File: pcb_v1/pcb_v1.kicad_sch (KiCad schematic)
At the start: 18 parts, among them SW2 SW_Push, U2 SRV05-4, U3 IQS624-3200-DNR

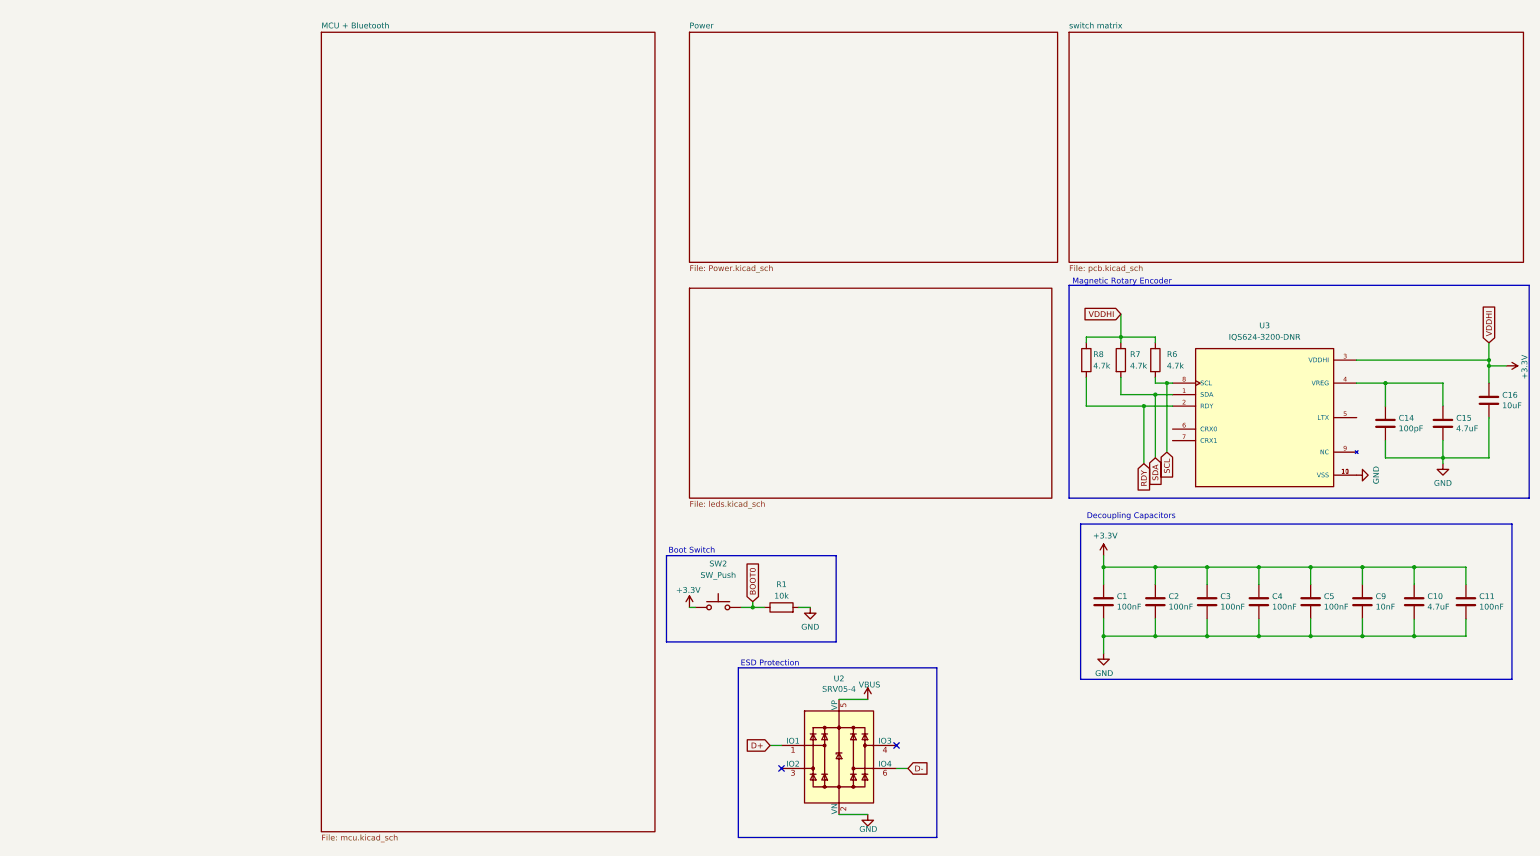
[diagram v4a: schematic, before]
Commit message: Connected OLED pin connector
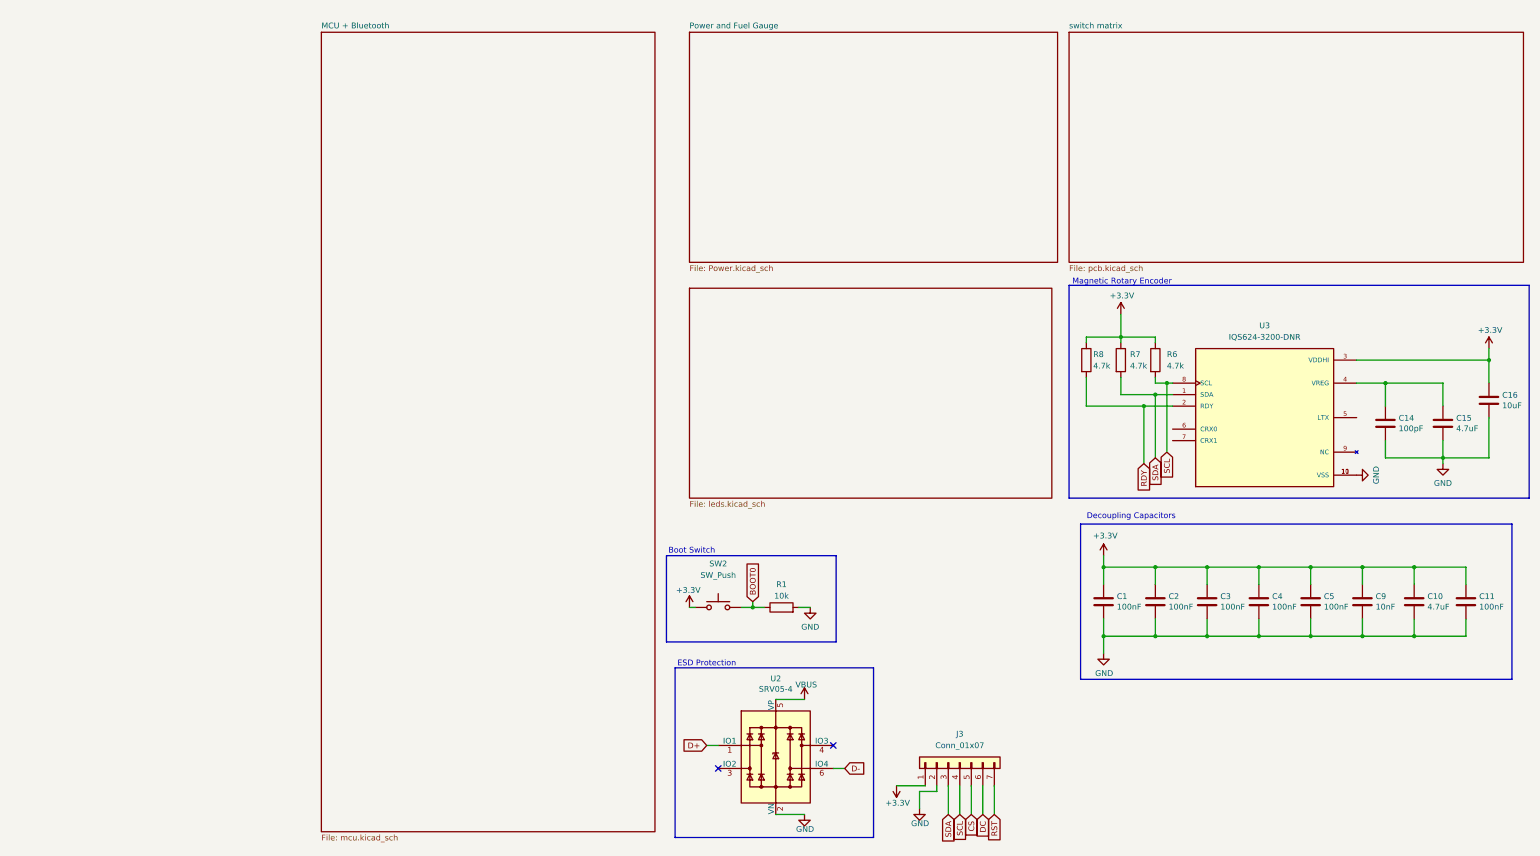
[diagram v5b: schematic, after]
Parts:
- added J3: Conn_01x07, Connector_JST:JST_SH_SM07B-SRSS-TB_1x07-1MP_P1.00mm_Horizontal, symbol Connector_Generic:Conn_01x07
- C1, C10, C11, C14, C15, C16, C2, C3, C4, C5, C9: footprint Murata Capacitor:CAPC1608X90N -> GRM1555C2A101GA01D:CAPC1005X55N
- R1, R6, R7, R8: footprint Yageo Resistor:RESC1607X60N -> RC0402FR-7D4K7L:RESC1005X40N
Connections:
- net +3.3V: now also J3.1 (Pin_1)
- net GND: now also J3.2 (Pin_2)
- net SCL: now also J3.4 (Pin_4)
- net SDA: now also J3.3 (Pin_3)
- new net CS: J3.5 (Pin_5)
- new net DC: J3.6 (Pin_6)
- new net RST: J3.7 (Pin_7)
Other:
- sheet Power renamed Power and Fuel Gauge
- moved on the sheet: U2

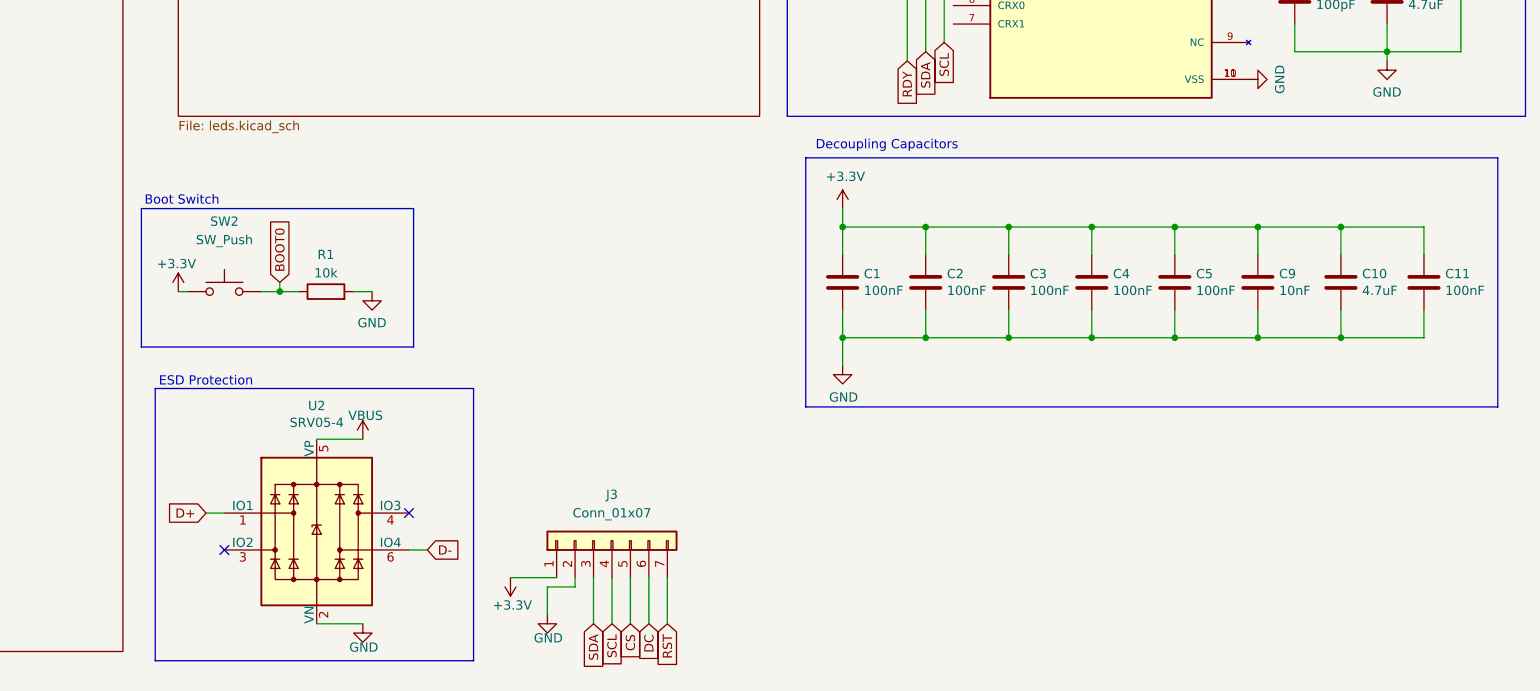
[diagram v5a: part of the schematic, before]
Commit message: Changed Layout of Keyboard
Row 1, Column 14 Removed due to OLED Screen taking up 2x2 u space
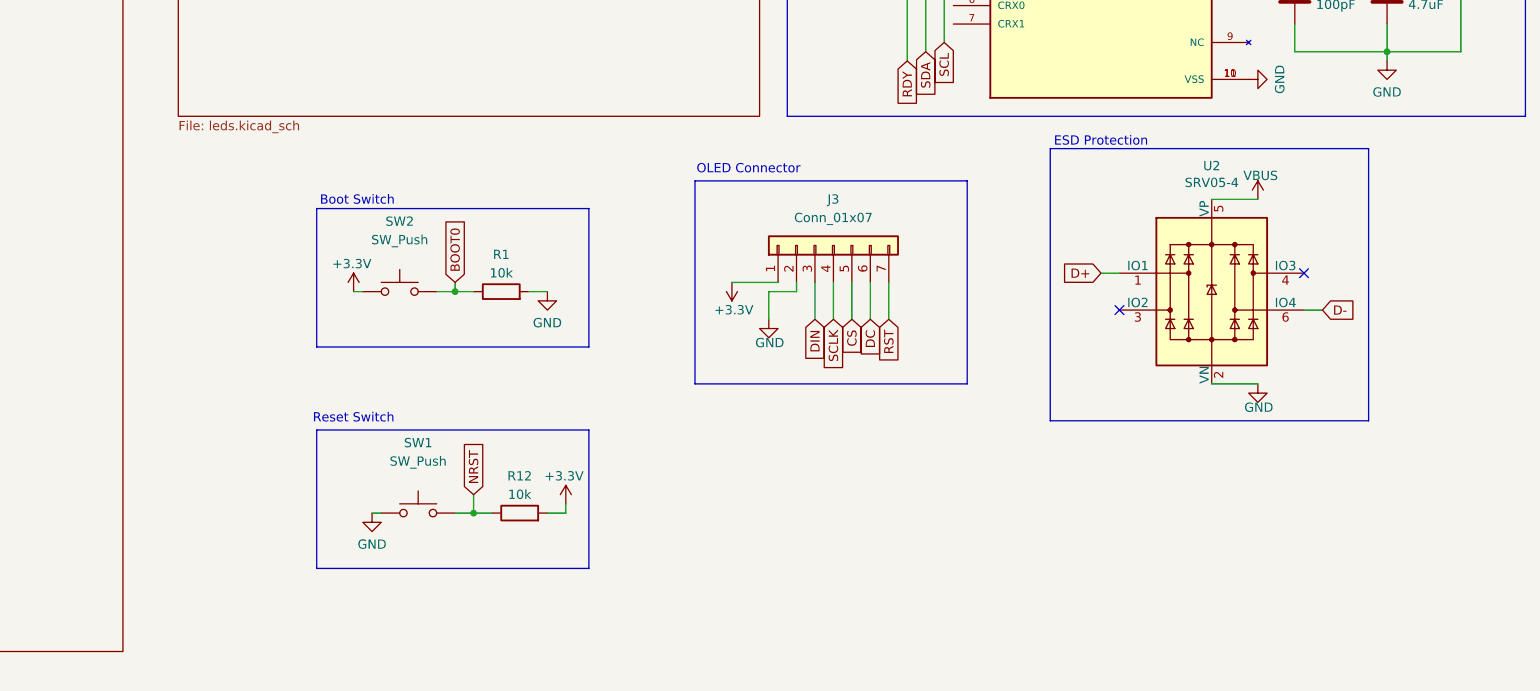
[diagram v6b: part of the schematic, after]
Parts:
- removed C1, C11, C2, C3, C4, C5: 100nF, GRM1555C2A101GA01D:CAPC1005X55N, symbol Device:C
- removed C10: 4.7uF, GRM1555C2A101GA01D:CAPC1005X55N, symbol Device:C
- removed C9: 10nF, GRM1555C2A101GA01D:CAPC1005X55N, symbol Device:C
- added R12: 10k, RC0402FR-7D4K7L:RESC1005X40N, symbol ScottoKeebs:Placeholder_Resistor
- added SW1: SW_Push, ScottoKeebs_Components:Button_TL3342, symbol Switch:SW_Push
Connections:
- net +3.3V: now also R12.2
- net GND: now also SW1.1
- net SCL: no longer J3.4 (Pin_4)
- net SDA: no longer J3.3 (Pin_3)
- new net DIN: J3.3 (Pin_3)
- new net NRST: R12.1, SW1.2
- new net SCLK: J3.4 (Pin_4)
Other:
- note added: "OLED Connector"
- note added: "Reset Switch"
- note removed: "Decoupling Capacitors"
- moved on the sheet: J3, R1, SW2, U2

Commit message: New Charger IC, Added Ground Plane
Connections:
- no-connect marks 2 -> 5
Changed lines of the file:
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@@
 		(at 254 143.51)
+	)
+	(no_connect
+		(at 205.74 106.68)
+	)
+	(no_connect
+		(at 205.74 109.22)
+	)
+	(no_connect
+		(at 246.38 104.14)
 	)
 	(wire

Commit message: Updated thru holes and connector sizings
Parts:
- J3: footprint Connector_JST:JST_SH_SM07B-SRSS-TB_1x07-1MP_P1.00mm_Horizontal -> Connector_JST:JST_PH_S7B-PH-SM4-TB_1x07-1MP_P2.00mm_Horizontal
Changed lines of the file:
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@@
 			)
 		)
-		(property "Footprint" "Connector_JST:JST_SH_SM07B-SRSS-TB_1x07-1MP_P1.00mm_Horizontal"
+		(property "Footprint" "Connector_JST:JST_PH_S7B-PH-SM4-TB_1x07-1MP_P2.00mm_Horizontal"
 			(at 189.23 139.7 0)
 			(effects
